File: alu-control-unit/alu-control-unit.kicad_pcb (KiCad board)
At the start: 2 copper layers, 346.7 x 55.9 mm, 14 parts, among them J1 Conn_01x08, J2 Conn_01x08, J3 Conn_01x04, J4 Conn_01x01, J5 Conn_01x08, J6 Conn_01x03, J7 PWR-2_pole_power_connector, U1 8-bit-bitwise-logic, U2 4-way-8-bit-bus-selector, U3 8_bit_xor, U4 8_bit_adder, U5 4-way-8-bit-bus-selector, U6 8-input-NOR

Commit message: Touch up ALU control unit PCB layout
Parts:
- added REF**: MountingHole_2.5mm_Pad, MountingHole:MountingHole_2.5mm_Pad, F.Cu at (364.5, 88.9)
- added REF**: MountingHole_2.5mm_Pad, MountingHole:MountingHole_2.5mm_Pad, F.Cu at (22.9, 88.9)
- J7 (x2): footprint emlun:J2x2-double_2_pole_connector -> emlun:PWR-double_2_pole_power_connector
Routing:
- net VCC: track 609.8 -> 613.4 mm
- net /a7: track 286.3 -> 288.9 mm
- net /a6: track 284.4 -> 286.5 mm
- net GND: track 610.1 -> 610.7 mm
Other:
- board text added: "CARRY_IN"
- board text added: "FLAGS"
- board text added: "O"
- board text added: "Os"
- board text added: "Ou"
- board text added: "Z"

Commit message: Touch up ALU control unit PCB layout
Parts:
- removed the REF** at (364.5, 88.9)
- removed the REF** at (22.9, 88.9)
- added REF**: MountingHole_2.2mm_M2_Pad, MountingHole:MountingHole_2.2mm_M2_Pad, F.Cu at (22.9, 88.9)
- added REF**: MountingHole_2.2mm_M2_Pad, MountingHole:MountingHole_2.2mm_M2_Pad, F.Cu at (364.5, 88.9)
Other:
- outline, holes or cut-outs redrawn
- board text added: "+"
- board text added: "0000: 0010: 0000: NOR 0001: NAND 0010: AND 0100: OR"
- board text added: "ALU control unit v1 Emil Lundberg emil@emlun.se 2018-08-02"
- board text added: "Addition result"
- board text added: "Addition unit"
- board text added: "Bitwise logic operation selector"
- board text added: "Bitwise logic result"
- board text added: "Bitwise logic unit"
- board text added: "Inputs A, B: Operands OP: Operation code CARRY_IN: Addition carry input"
- board text added: "Master output"
- board text added: "OP"
- board text added: "Outputs O: Result Ou: Unsigned overflow Os: Signed overflow Z: Zero output"
- board text added: "Selection"
- board text added: "Subsystem selector"
- board text added: "Unassigned"
- board text added: "XOR result"
- board text added: "XOR unit"
- board text added: "Zero output detector"
- board text added: "∧"
- board text added: "∨"
- board text added: "⊻"
- board text added: "⊼"
- board text added: "⊽"
- board text removed: "INS"

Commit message: Rearrange 8-input NOR footprint to match the working prototype
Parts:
- moved U6 5.08 mm to (144.8, 81.3)
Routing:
- net VCC: track 613.4 -> 636.6 mm
- net /out_zero: track 19.6 -> 36.6 mm, vias 1 -> 0
- net GND: track 610.7 -> 617.8 mm, vias 3 -> 2
- net /out7: track 158.5 -> 163.8 mm, vias 2 -> 3
- net /out6: track 158.6 -> 163.7 mm
- net /out5: track 159.3 -> 164.4 mm
- net /out4: track 159.9 -> 165.0 mm
- net /out2: track 161.2 -> 166.3 mm
- net /out1: track 161.8 -> 166.9 mm
- net /out0: track 163.1 -> 167.5 mm
- net /ins3: track 167.1 -> 164.8 mm
- net /ins2: track 167.1 -> 164.8 mm
- net /ins1: track 220.8 -> 218.5 mm
- net /ins0: track 214.4 -> 212.2 mm
- net /out3: track 163.7 -> 165.6 mm
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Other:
- board text added: "0000: Addition 0001: Addition 0010: Addition 0011: Addition 0100: XOR 0101: XOR 0110: XOR 0111: XOR 1000: NOR 1001: NAND 1010: AND 1011: OR 1100: Unassigned 1101: Unassigned 1110: Unassigned 1111: Unassigned"
- board text added: "Inputs A, B: Operands OP: Operation code CARRY_IN: Addition carry"
- board text removed: "0000: 0010: 0000: NOR 0001: NAND 0010: AND 0100: OR"
- board text removed: "Inputs A, B: Operands OP: Operation code CARRY_IN: Addition carry input"

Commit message: Touch up ALU control unit PCB layout
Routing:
- net /a7: track 289.4 -> 281.5 mm
- net /a6: track 287.0 -> 282.2 mm
- net VCC: track 636.6 -> 632.9 mm
- net /a5: track 279.4 -> 277.8 mm
- net /a2: track 279.1 -> 277.8 mm
- net /a1: track 279.1 -> 277.8 mm
- net /b5: track 282.7 -> 281.4 mm
- net /b7: track 282.7 -> 281.4 mm
- net /b6: track 282.7 -> 281.4 mm
- net /b2: track 282.1 -> 280.8 mm
- net /b1: track 281.4 -> 280.1 mm
- net /a3: track 279.1 -> 277.8 mm
- net /a0: track 279.1 -> 277.8 mm
- net /b3: track 282.7 -> 281.4 mm
- net /b0: track 280.2 -> 278.9 mm
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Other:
- board text added: "0000: Addition 0100: XOR 1000: NOR 1001: NAND 1010: AND 1011: OR 1100: Unassigned"
- board text added: "ALU control unit v1 Emil Lundberg emil@emlun.se 2018-08-04"
- board text removed: "0000: Addition 0001: Addition 0010: Addition 0011: Addition 0100: XOR 0101: XOR 0110: XOR 0111: XOR 1000: NOR 1001: NAND 1010: AND 1011: OR 1100: Unassigned 1101: Unassigned 1110: Unassigned 1111: Unassigned"
- board text removed: "ALU control unit v1 Emil Lundberg emil@emlun.se 2018-08-02"

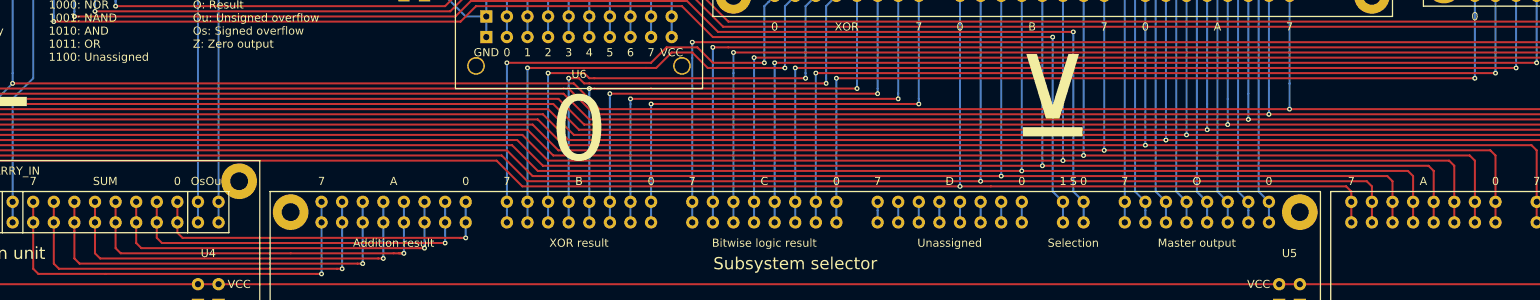
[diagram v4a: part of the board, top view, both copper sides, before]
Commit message: Update ALU PCB layout with new operation code
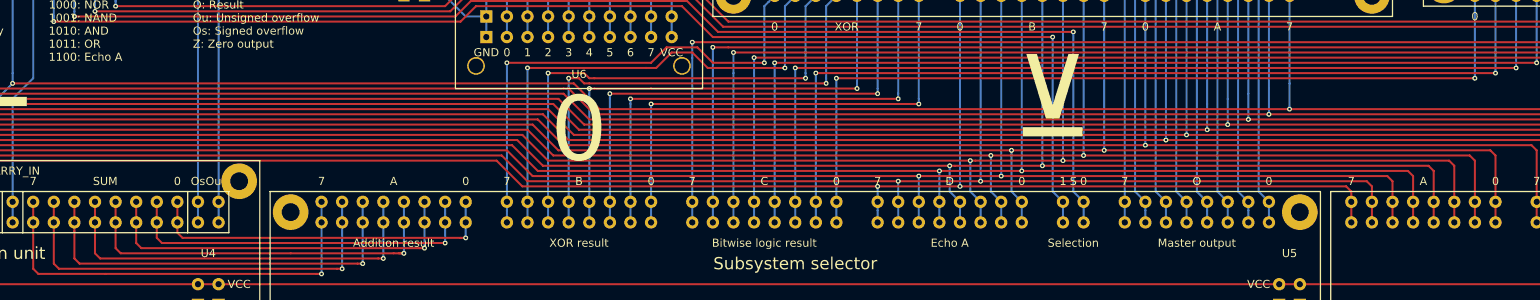
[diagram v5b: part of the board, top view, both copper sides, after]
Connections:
- U5 pad 25: Net-(U5-Pad25) -> /a7
- U5 pad 26: Net-(U5-Pad26) -> /a6
- U5 pad 27: Net-(U5-Pad27) -> /a5
- U5 pad 28: Net-(U5-Pad28) -> /a4
- U5 pad 29: Net-(U5-Pad29) -> /a3
- U5 pad 30: Net-(U5-Pad30) -> /a2
- U5 pad 31: Net-(U5-Pad31) -> /a1
- U5 pad 32: Net-(U5-Pad32) -> /a0
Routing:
- net /a0: track 277.8 -> 287.2 mm, vias 2 -> 3
- net /a1: track 277.8 -> 286.6 mm, vias 2 -> 3
- net /a2: track 277.8 -> 285.9 mm, vias 2 -> 3
- net /a3: track 277.8 -> 285.3 mm, vias 2 -> 3
- net /a4: track 277.8 -> 284.2 mm, vias 2 -> 3
- net /a5: track 277.8 -> 283.5 mm, vias 2 -> 3
- net /a6: track 282.2 -> 287.3 mm, vias 2 -> 3
- net /a7: track 281.5 -> 285.9 mm, vias 2 -> 3
- net Net-(U5-Pad32): track 2.54 -> 0.00 mm
- net Net-(U5-Pad31): track 2.54 -> 0.00 mm
- net Net-(U5-Pad30): track 2.54 -> 0.00 mm
- net Net-(U5-Pad29): track 2.54 -> 0.00 mm
- net Net-(U5-Pad28): track 2.54 -> 0.00 mm
- net Net-(U5-Pad27): track 2.54 -> 0.00 mm
- net Net-(U5-Pad26): track 2.54 -> 0.00 mm
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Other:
- board text added: "0000: Addition 0100: XOR 1000: NOR 1001: NAND 1010: AND 1011: OR 1100: Echo A"
- board text added: "Echo A"
- board text removed: "0000: Addition 0100: XOR 1000: NOR 1001: NAND 1010: AND 1011: OR 1100: Unassigned"
- board text removed: "Unassigned"

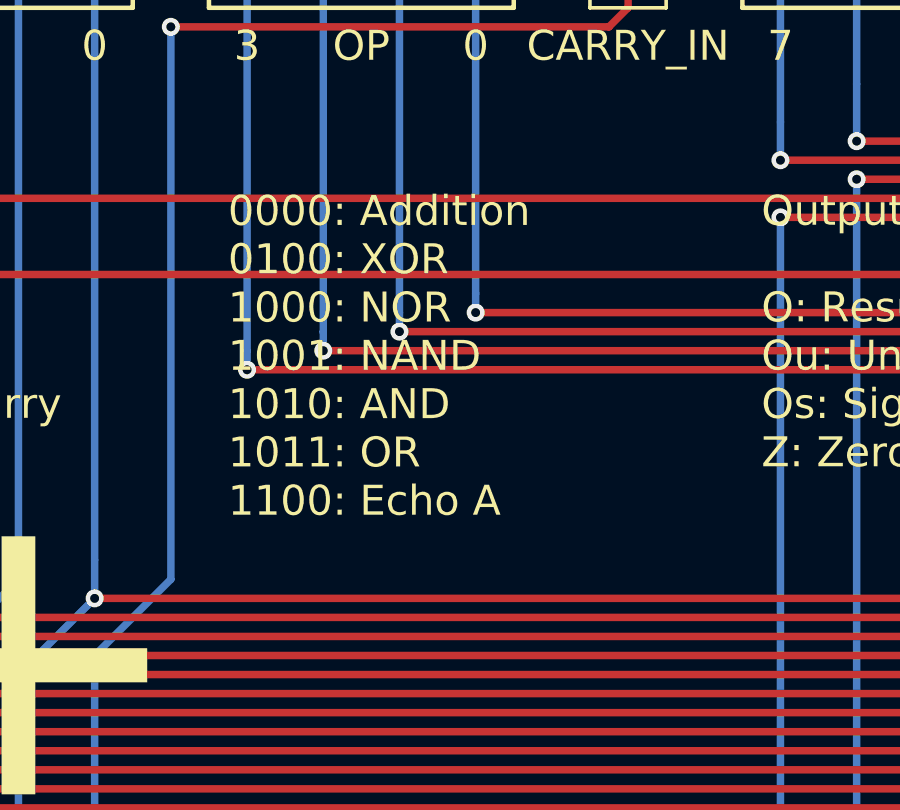
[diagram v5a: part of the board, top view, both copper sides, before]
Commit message: Touch up ALU control unit PCB layout
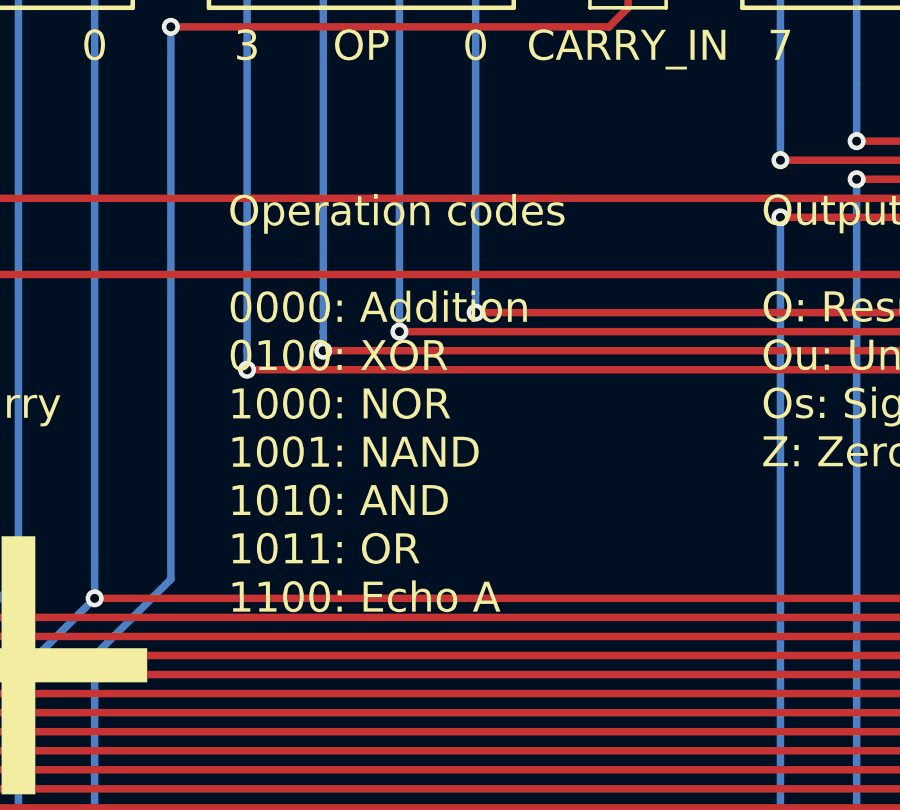
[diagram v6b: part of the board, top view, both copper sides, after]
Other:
- board text added: "Operation codes 0000: Addition 0100: XOR 1000: NOR 1001: NAND 1010: AND 1011: OR 1100: Echo A"
- board text removed: "0000: Addition 0100: XOR 1000: NOR 1001: NAND 1010: AND 1011: OR 1100: Echo A"

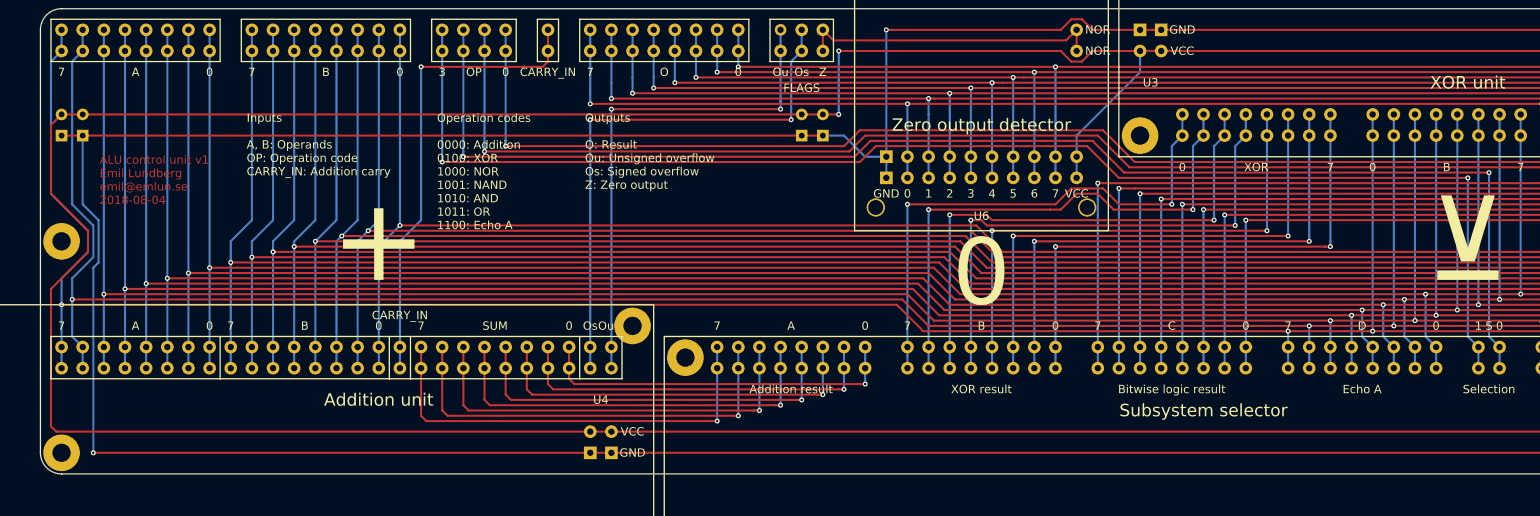
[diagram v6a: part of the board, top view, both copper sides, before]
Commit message: Wire up ALU pull-down resistors
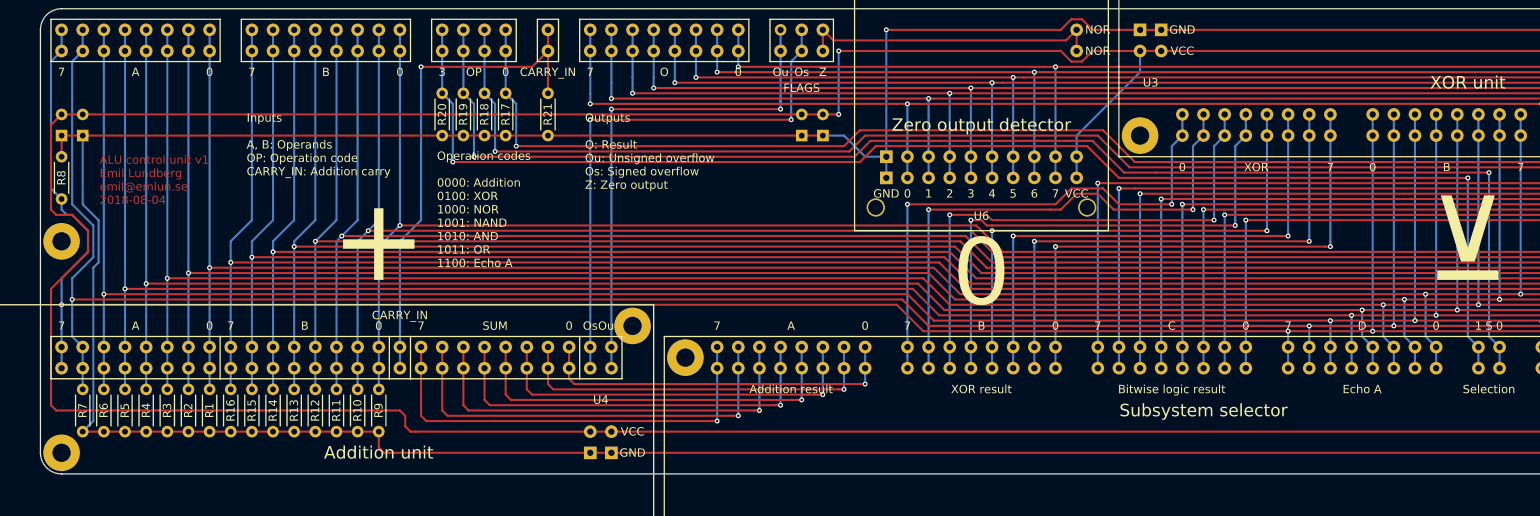
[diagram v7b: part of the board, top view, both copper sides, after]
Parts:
- added R1: R, emlun:R_Axial_DIN0204_L3.6mm_D1.6mm_P5.08mm_Horizontal, F.Cu at (40.6, 111.8)
- added R10: R, emlun:R_Axial_DIN0204_L3.6mm_D1.6mm_P5.08mm_Horizontal, F.Cu at (58.4, 111.8)
- added R11: R, emlun:R_Axial_DIN0204_L3.6mm_D1.6mm_P5.08mm_Horizontal, F.Cu at (55.9, 111.8)
- added R12: R, emlun:R_Axial_DIN0204_L3.6mm_D1.6mm_P5.08mm_Horizontal, F.Cu at (53.3, 111.8)
- added R13: R, emlun:R_Axial_DIN0204_L3.6mm_D1.6mm_P5.08mm_Horizontal, F.Cu at (50.8, 111.8)
- added R14: R, emlun:R_Axial_DIN0204_L3.6mm_D1.6mm_P5.08mm_Horizontal, F.Cu at (48.3, 111.8)
- added R15: R, emlun:R_Axial_DIN0204_L3.6mm_D1.6mm_P5.08mm_Horizontal, F.Cu at (45.7, 111.8)
- added R16: R, emlun:R_Axial_DIN0204_L3.6mm_D1.6mm_P5.08mm_Horizontal, F.Cu at (43.2, 111.8)
- added R17: R, emlun:R_Axial_DIN0204_L3.6mm_D1.6mm_P5.08mm_Horizontal, F.Cu at (76.2, 76.2)
- added R18: R, emlun:R_Axial_DIN0204_L3.6mm_D1.6mm_P5.08mm_Horizontal, F.Cu at (73.7, 76.2)
- added R19: R, emlun:R_Axial_DIN0204_L3.6mm_D1.6mm_P5.08mm_Horizontal, F.Cu at (71.1, 76.2)
- added R2: R, emlun:R_Axial_DIN0204_L3.6mm_D1.6mm_P5.08mm_Horizontal, F.Cu at (38.1, 111.8)
- added R20: R, emlun:R_Axial_DIN0204_L3.6mm_D1.6mm_P5.08mm_Horizontal, F.Cu at (68.6, 76.2)
- added R21: R, emlun:R_Axial_DIN0204_L3.6mm_D1.6mm_P5.08mm_Horizontal, F.Cu at (81.3, 76.2)
- added R3: R, emlun:R_Axial_DIN0204_L3.6mm_D1.6mm_P5.08mm_Horizontal, F.Cu at (35.6, 111.8)
- added R4: R, emlun:R_Axial_DIN0204_L3.6mm_D1.6mm_P5.08mm_Horizontal, F.Cu at (33.0, 111.8)
- added R5: R, emlun:R_Axial_DIN0204_L3.6mm_D1.6mm_P5.08mm_Horizontal, F.Cu at (30.5, 111.8)
- added R6: R, emlun:R_Axial_DIN0204_L3.6mm_D1.6mm_P5.08mm_Horizontal, F.Cu at (27.9, 111.8)
- added R7: R, emlun:R_Axial_DIN0204_L3.6mm_D1.6mm_P5.08mm_Horizontal, F.Cu at (25.4, 111.8)
- added R8: R, emlun:R_Axial_DIN0204_L3.6mm_D1.6mm_P5.08mm_Horizontal, F.Cu at (22.9, 78.7)
- added R9: R, emlun:R_Axial_DIN0204_L3.6mm_D1.6mm_P5.08mm_Horizontal, F.Cu at (61.0, 111.8)
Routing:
- net /carry_in: track 56.6 -> 60.9 mm
- net GND: track 617.8 -> 621.8 mm, vias 2 -> 1
- net /b7: track 281.4 -> 283.9 mm
- net /b6: track 281.4 -> 283.9 mm
- net /b5: track 281.4 -> 283.9 mm
- net /b4: track 281.4 -> 283.9 mm
- net /b3: track 281.4 -> 283.9 mm
- net /b2: track 280.8 -> 283.3 mm
- net /b1: track 280.1 -> 282.7 mm
- net /b0: track 278.9 -> 281.4 mm
- net /a5: track 283.5 -> 286.1 mm
- net /a4: track 284.2 -> 286.7 mm
- net /a6: track 287.3 -> 289.8 mm
- net /a3: track 285.3 -> 287.9 mm
- net /a2: track 285.9 -> 288.5 mm
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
